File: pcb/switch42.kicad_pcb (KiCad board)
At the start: 2 copper layers, 91 x 55 mm, 27 parts, among them SW1 SW_PUSH, SW10 SW_PUSH, SW2 SW_PUSH, SW3 SW_PUSH, SW4 SW_PUSH, SW5 SW_PUSH, SW6 SW_PUSH, SW8 SW_PUSH, SW9 SW_PUSH, U1 ProMicro

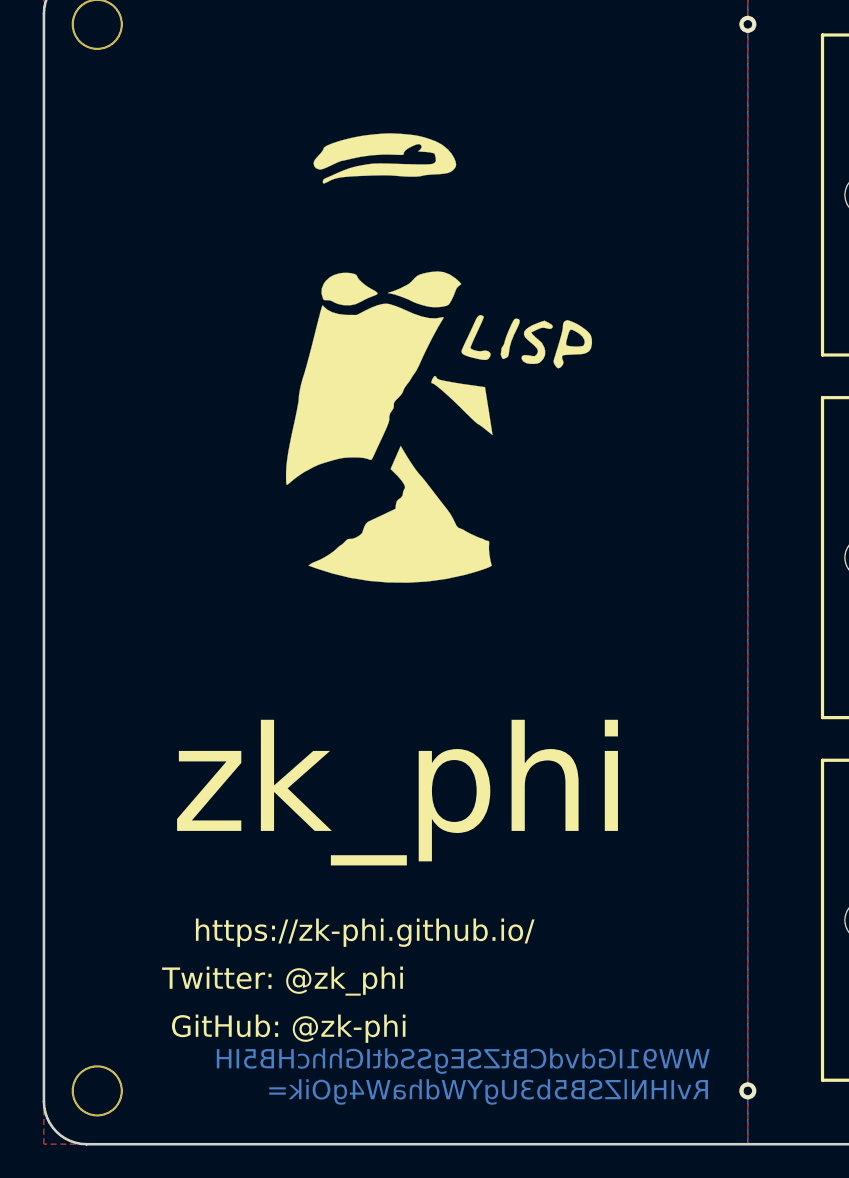
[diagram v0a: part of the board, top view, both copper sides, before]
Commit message: Move meishi contents slightly upward
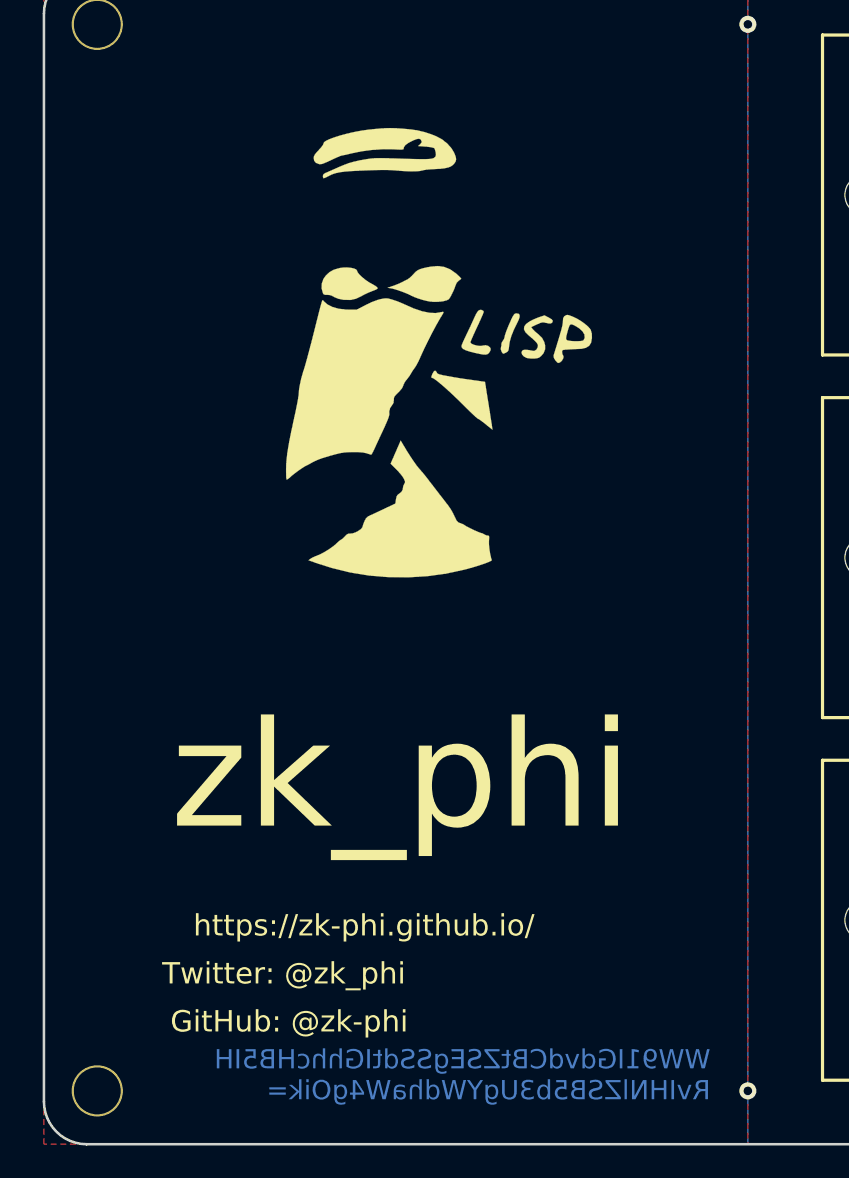
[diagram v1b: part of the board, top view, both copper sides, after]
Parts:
- moved G*** 0.25 mm to (66.8, 66.5) (x2)
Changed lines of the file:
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@@
   )
   (module paripi:Untitled2 (layer F.Cu)
-    (at 66.75 66.75)
+    (at 66.75 66.5)
     (fp_text reference G*** (at 0 0) (layer F.SilkS) hide
       (effects (font (size 1.524 1.524) (thickness 0.3)))
@@
   )
   (module paripi:Untitled (layer F.Cu)
-    (at 66.75 66.75)
+    (at 66.75 66.5)
     (fp_text reference G*** (at 0 0) (layer F.SilkS) hide
       (effects (font (size 1.524 1.524) (thickness 0.3)))
@@
       (xy -0.244517 -0.11784) (xy -0.229978 -0.100089) (xy -0.224367 -0.096087) (xy -0.217842 -0.102074)) (layer B.SilkS) (width 0.01))
   )
-  (gr_text "GitHub: @zk-phi" (at 61.5 99.5) (layer F.SilkS)
+  (gr_text "GitHub: @zk-phi" (at 61.5 99.25) (layer F.SilkS)
     (effects (font (size 1 1) (thickness 0.2)))
   )
-  (gr_text "Twitter: @zk_phi" (at 61.25 97.25) (layer F.SilkS)
+  (gr_text "Twitter: @zk_phi" (at 61.25 97) (layer F.SilkS)
     (effects (font (size 1 1) (thickness 0.2)))
   )
@@
   (gr_line (start 95.75 62.75) (end 95.75 67.25) (layer Edge.Cuts) (width 0.12))
   (gr_line (start 92.25 62.75) (end 95.75 62.75) (layer Edge.Cuts) (width 0.12))
-  (gr_line (start 78.75 100.5) (end 54.75 100.5) (layer Cmts.User) (width 0.6))
-  (gr_line (start 78.75 54.5) (end 78.75 100.5) (layer Cmts.User) (width 0.6))
-  (gr_line (start 54.75 54.5) (end 78.75 54.5) (layer Cmts.User) (width 0.6))
-  (gr_line (start 54.75 100.5) (end 54.75 54.5) (layer Cmts.User) (width 0.6))
-  (gr_text "Software Engineer" (at 66.75 83) (layer F.Mask)
+  (gr_line (start 78.75 100.25) (end 54.75 100.25) (layer Cmts.User) (width 0.6))
+  (gr_line (start 78.75 54.25) (end 78.75 100.25) (layer Cmts.User) (width 0.6))
+  (gr_line (start 54.75 54.25) (end 78.75 54.25) (layer Cmts.User) (width 0.6))
+  (gr_line (start 54.75 100.25) (end 54.75 54.25) (layer Cmts.User) (width 0.6))
+  (gr_text "Software Engineer" (at 66.75 82.75) (layer F.Mask)
     (effects (font (size 1.7 1.7) (thickness 0.3)))
   )
-  (gr_text https://zk-phi.github.io/ (at 65 95) (layer F.SilkS)
+  (gr_text https://zk-phi.github.io/ (at 65 94.75) (layer F.SilkS)
     (effects (font (size 1 1) (thickness 0.2)))
   )
-  (gr_text zk_phi (at 66.75 88) (layer F.SilkS)
+  (gr_text zk_phi (at 66.75 87.75) (layer F.SilkS)
     (effects (font (size 5 5) (thickness 0.7)))
   )

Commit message: Get screw holes plated
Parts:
- Ref** (x4): footprint phi-kbd-library:M2_SCREW_HOLE -> phi-kbd-library:M2_SCREW_HOLE_Plated
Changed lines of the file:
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@@
     (add_net sw9)
+  )
+  (module phi-kbd-library:M2_SCREW_HOLE_Plated (layer F.Cu)
+    (at 138.5 52.5)
+    (descr "Mounting Hole 2.2mm, no annular, M2")
+    (tags "mounting hole 2.2mm no annular m2")
+    (attr virtual)
+    (fp_text reference Ref** (at 0 -3.2) (layer F.Fab)
+      (effects (font (size 1 1) (thickness 0.15)))
+    )
+    (fp_text value Val** (at 0 3.2) (layer F.Fab)
+      (effects (font (size 1 1) (thickness 0.15)))
+    )
+    (fp_circle (center 0 0) (end 0 1.75) (layer F.Fab) (width 0.15))
+    (fp_text user %R (at 0.3 0) (layer F.Fab)
+      (effects (font (size 1 1) (thickness 0.15)))
+    )
+    (pad "" thru_hole circle (at 0 0) (size 2.4 2.4) (drill 2.2) (layers *.Cu *.Mask))
+    (model ${KISYS3DMOD}/phi-kbd.3dshapes/M2_Screw.step
+      (at (xyz 0 0 0))
+      (scale (xyz 1 1 1))
+      (rotate (xyz 0 0 0))
+    )
+  )
+  (module phi-kbd-library:M2_SCREW_HOLE_Plated (layer F.Cu)
+    (at 138.5 102.5)
+    (descr "Mounting Hole 2.2mm, no annular, M2")
+    (tags "mounting hole 2.2mm no annular m2")
+    (attr virtual)
+    (fp_text reference Ref** (at 0 -3.2) (layer F.Fab)
+      (effects (font (size 1 1) (thickness 0.15)))
+    )
+    (fp_text value Val** (at 0 3.2) (layer F.Fab)
+      (effects (font (size 1 1) (thickness 0.15)))
+    )
+    (fp_circle (center 0 0) (end 0 1.75) (layer F.Fab) (width 0.15))
+    (fp_text user %R (at 0.3 0) (layer F.Fab)
+      (effects (font (size 1 1) (thickness 0.15)))
+    )
+    (pad "" thru_hole circle (at 0 0) (size 2.4 2.4) (drill 2.2) (layers *.Cu *.Mask))
+    (model ${KISYS3DMOD}/phi-kbd.3dshapes/M2_Screw.step
+      (at (xyz 0 0 0))
+      (scale (xyz 1 1 1))
+      (rotate (xyz 0 0 0))
+    )
+  )
+  (module phi-kbd-library:M2_SCREW_HOLE_Plated (layer F.Cu)
+    (at 52.5 102.5)
+    (descr "Mounting Hole 2.2mm, no annular, M2")
+    (tags "mounting hole 2.2mm no annular m2")
+    (attr virtual)
+    (fp_text reference Ref** (at 0 -3.2) (layer F.Fab)
+      (effects (font (size 1 1) (thickness 0.15)))
+    )
+    (fp_text value Val** (at 0 3.2) (layer F.Fab)
+      (effects (font (size 1 1) (thickness 0.15)))
+    )
+    (fp_circle (center 0 0) (end 0 1.75) (layer F.Fab) (width 0.15))
+    (fp_text user %R (at 0.3 0) (layer F.Fab)
+      (effects (font (size 1 1) (thickness 0.15)))
+    )
+    (pad "" thru_hole circle (at 0 0) (size 2.4 2.4) (drill 2.2) (layers *.Cu *.Mask))
+    (model ${KISYS3DMOD}/phi-kbd.3dshapes/M2_Screw.step
+      (at (xyz 0 0 0))
+      (scale (xyz 1 1 1))
+      (rotate (xyz 0 0 0))
+    )
+  )
+  (module phi-kbd-library:M2_SCREW_HOLE_Plated (layer F.Cu)
+    (at 52.5 52.5)
+    (descr "Mounting Hole 2.2mm, no annular, M2")
+    (tags "mounting hole 2.2mm no annular m2")
+    (attr virtual)
+    (fp_text reference Ref** (at 0 -3.2) (layer F.Fab)
+      (effects (font (size 1 1) (thickness 0.15)))
+    )
+    (fp_text value Val** (at 0 3.2) (layer F.Fab)
+      (effects (font (size 1 1) (thickness 0.15)))
+    )
+    (fp_circle (center 0 0) (end 0 1.75) (layer F.Fab) (width 0.15))
+    (fp_text user %R (at 0.3 0) (layer F.Fab)
+      (effects (font (size 1 1) (thickness 0.15)))
+    )
+    (pad "" thru_hole circle (at 0 0) (size 2.4 2.4) (drill 2.2) (layers *.Cu *.Mask))
+    (model ${KISYS3DMOD}/phi-kbd.3dshapes/M2_Screw.step
+      (at (xyz 0 0 0))
+      (scale (xyz 1 1 1))
+      (rotate (xyz 0 0 0))
+    )
   )
   (module paripi:Untitled2 (layer F.Cu)
@@
     )
   )
-  (module phi-kbd-library:M2_SCREW_HOLE (layer F.Cu)
-    (at 52.5 52.5)
-    (descr "Mounting Hole 2.2mm, no annular, M2")
-    (tags "mounting hole 2.2mm no annular m2")
-    (attr virtual)
-    (fp_text reference Ref** (at 0 -3.2) (layer F.Fab)
-      (effects (font (size 1 1) (thickness 0.15)))
-    )
-    (fp_text value Val** (at 0 3.2) (layer F.Fab)
-      (effects (font (size 1 1) (thickness 0.15)))
-    )
-    (fp_circle (center 0 0) (end 0 1.75) (layer F.Fab) (width 0.15))
-    (fp_text user %R (at 0.3 0) (layer F.Fab)
-      (effects (font (size 1 1) (thickness 0.15)))
-    )
-    (pad "" np_thru_hole circle (at 0 0) (size 2.4 2.4) (drill 2.2) (layers *.Cu *.Mask))
-    (model ${KISYS3DMOD}/phi-kbd.3dshapes/M2_Screw.step
-      (at (xyz 0 0 0))
-      (scale (xyz 1 1 1))
-      (rotate (xyz 0 0 0))
-    )
-  )
-  (module phi-kbd-library:M2_SCREW_HOLE (layer F.Cu)
-    (at 138.5 52.5)
-    (descr "Mounting Hole 2.2mm, no annular, M2")
-    (tags "mounting hole 2.2mm no annular m2")
-    (attr virtual)
-    (fp_text reference Ref** (at 0 -3.2) (layer F.Fab)
-      (effects (font (size 1 1) (thickness 0.15)))
-    )
-    (fp_text value Val** (at 0 3.2) (layer F.Fab)
-      (effects (font (size 1 1) (thickness 0.15)))
-    )
-    (fp_circle (center 0 0) (end 0 1.75) (layer F.Fab) (width 0.15))
-    (fp_text user %R (at 0.3 0) (layer F.Fab)
-      (effects (font (size 1 1) (thickness 0.15)))
-    )
-    (pad "" np_thru_hole circle (at 0 0) (size 2.4 2.4) (drill 2.2) (layers *.Cu *.Mask))
-    (model ${KISYS3DMOD}/phi-kbd.3dshapes/M2_Screw.step
-      (at (xyz 0 0 0))
-      (scale (xyz 1 1 1))
-      (rotate (xyz 0 0 0))
-    )
-  )
-  (module phi-kbd-library:M2_SCREW_HOLE (layer F.Cu)
-    (at 52.5 102.5)
-    (descr "Mounting Hole 2.2mm, no annular, M2")
-    (tags "mounting hole 2.2mm no annular m2")
-    (attr virtual)
-    (fp_text reference Ref** (at 0 -3.2) (layer F.Fab)
-      (effects (font (size 1 1) (thickness 0.15)))
-    )
-    (fp_text value Val** (at 0 3.2) (layer F.Fab)
-      (effects (font (size 1 1) (thickness 0.15)))
-    )
-    (fp_circle (center 0 0) (end 0 1.75) (layer F.Fab) (width 0.15))
-    (fp_text user %R (at 0.3 0) (layer F.Fab)
-      (effects (font (size 1 1) (thickness 0.15)))
-    )
-    (pad "" np_thru_hole circle (at 0 0) (size 2.4 2.4) (drill 2.2) (layers *.Cu *.Mask))
-    (model ${KISYS3DMOD}/phi-kbd.3dshapes/M2_Screw.step
-      (at (xyz 0 0 0))
-      (scale (xyz 1 1 1))
-      (rotate (xyz 0 0 0))
-    )
-  )
-  (module phi-kbd-library:M2_SCREW_HOLE (layer F.Cu)
-    (at 138.5 102.5)
-    (descr "Mounting Hole 2.2mm, no annular, M2")
-    (tags "mounting hole 2.2mm no annular m2")
-    (attr virtual)
-    (fp_text reference Ref** (at 0 -3.2) (layer F.Fab)
-      (effects (font (size 1 1) (thickness 0.15)))
-    )
-    (fp_text value Val** (at 0 3.2) (layer F.Fab)
-      (effects (font (size 1 1) (thickness 0.15)))
-    )
-    (fp_circle (center 0 0) (end 0 1.75) (layer F.Fab) (width 0.15))
-    (fp_text user %R (at 0.3 0) (layer F.Fab)
-      (effects (font (size 1 1) (thickness 0.15)))
-    )
-    (pad "" np_thru_hole circle (at 0 0) (size 2.4 2.4) (drill 2.2) (layers *.Cu *.Mask))
-    (model ${KISYS3DMOD}/phi-kbd.3dshapes/M2_Screw.step
-      (at (xyz 0 0 0))
-      (scale (xyz 1 1 1))
-      (rotate (xyz 0 0 0))
-    )
-  )
   (module phi-kbd-library:Icon-Scissors (layer B.Cu)
     (at 109.25 54.5 270)
@@
   (gr_line (start 54.75 54.25) (end 78.75 54.25) (layer Cmts.User) (width 0.6))
   (gr_line (start 54.75 100.25) (end 54.75 54.25) (layer Cmts.User) (width 0.6))
-  (gr_text "Software Engineer" (at 66.75 82.75) (layer F.Mask)
+  (gr_text "Software Engineer" (at 66.75 82.5) (layer F.Mask)
     (effects (font (size 1.7 1.7) (thickness 0.3)))
   )

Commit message: Update challenge
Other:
- board text added: "D1"
- board text added: "D2"
- board text added: "D3"
- board text added: "D4"
- board text added: "D5"
- board text added: "D6"
- board text added: "D7"
- board text added: "D8"
- board text added: "D9"
- board text added: "GRID = .25"
- board text added: "“64” and “13” me ! (I = ai) SFVIIDB6ciBMMXINCmdjbiAwY3 QgVDQ0DQp+RiEgcjJhIFpsMQ=="
- board text removed: "WW91IGdvdCBtZSEgSSdtIGhhcHB5IH RvIHNlZSB5b3UgYWdhaW4gOik="
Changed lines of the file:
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@@
   (general
     (thickness 1.6)
-    (drawings 67)
+    (drawings 77)
     (tracks 112)
     (zones 0)
@@
       (xy -0.244517 -0.11784) (xy -0.229978 -0.100089) (xy -0.224367 -0.096087) (xy -0.217842 -0.102074)) (layer B.SilkS) (width 0.01))
   )
+  (gr_text D9 (at 134.75 99) (layer B.SilkS)
+    (effects (font (size 1 1) (thickness 0.2)) (justify mirror))
+  )
+  (gr_text D8 (at 116.75 99) (layer B.SilkS)
+    (effects (font (size 1 1) (thickness 0.2)) (justify mirror))
+  )
+  (gr_text D7 (at 98.75 99) (layer B.SilkS)
+    (effects (font (size 1 1) (thickness 0.2)) (justify mirror))
+  )
+  (gr_text D6 (at 134.75 82) (layer B.SilkS)
+    (effects (font (size 1 1) (thickness 0.2)) (justify mirror))
+  )
+  (gr_text D5 (at 116.75 82) (layer B.SilkS)
+    (effects (font (size 1 1) (thickness 0.2)) (justify mirror))
+  )
+  (gr_text D4 (at 98.75 82) (layer B.SilkS)
+    (effects (font (size 1 1) (thickness 0.2)) (justify mirror))
+  )
+  (gr_text D3 (at 134.75 65) (layer B.SilkS)
+    (effects (font (size 1 1) (thickness 0.2)) (justify mirror))
+  )
+  (gr_text D2 (at 116.75 65) (layer B.SilkS)
+    (effects (font (size 1 1) (thickness 0.2)) (justify mirror))
+  )
+  (gr_text D1 (at 98.75 65) (layer B.SilkS)
+    (effects (font (size 1 1) (thickness 0.2)) (justify mirror))
+  )
+  (gr_text "GRID = .25" (at 133.75 107.75) (layer Dwgs.User)
+    (effects (font (size 1.5 1.5) (thickness 0.3)))
+  )
   (gr_text "GitHub: @zk-phi" (at 61.5 99.25) (layer F.SilkS)
     (effects (font (size 1 1) (thickness 0.2)))
@@
     (effects (font (size 1 0.9) (thickness 0.2)) (justify mirror))
   )
-  (gr_text "WW91IGdvdCBtZSEgSSdtIGhhcHB5IH\nRvIHNlZSB5b3UgYWdhaW4gOik=" (at 81.25 101.75) (layer B.Cu)
+  (gr_text "“64” and “13” me ! (I = ai)\nSFVIIDB6ciBMMXINCmdjbiAwY3\nQgVDQ0DQp+RiEgcjJhIFpsMQ==" (at 81.25 100.75) (layer B.Cu)
     (effects (font (size 0.9 0.9) (thickness 0.2)) (justify left mirror))
   )
@@
   (gr_line (start 54.75 54.25) (end 78.75 54.25) (layer Cmts.User) (width 0.6))
   (gr_line (start 54.75 100.25) (end 54.75 54.25) (layer Cmts.User) (width 0.6))
-  (gr_text "Software Engineer" (at 66.75 82.5) (layer F.Mask)
+  (gr_text "Software Engineer" (at 66.75 82.25) (layer F.Mask)
     (effects (font (size 1.7 1.7) (thickness 0.3)))
   )
@@
     (effects (font (size 1 1) (thickness 0.2)))
   )
-  (gr_text zk_phi (at 66.75 87.75) (layer F.SilkS)
+  (gr_text zk_phi (at 66.75 88) (layer F.SilkS)
     (effects (font (size 5 5) (thickness 0.7)))
   )

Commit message: Update buildguide
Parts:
- removed the G*** at (109.2, 54.5)
- removed the G*** at (114.2, 56.8)
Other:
- board text added: "1. Flash the firmware on a ProMicro available here: https://github.com/zk-phi/qmk_firmware $ sh util/<your_OS>_install.sh $ make handwired/ddm9:default:avrdude 2. Solder x9 SK6812mini LEDs (Optional) * connected in serial D1 > D2 > … 3. Solder x9 Kailh Choc switches * cut pins marked with “X” 4. Plug ProMicro in with “Conthrough”s"
- board text added: "Build your keypad !"
- board text added: "X"
- board text added: "“64” and “13” me ! (I = “ai”) SFVIIDB6ciBMMXINCmdjbiAwY3 QgVDQ0DQp+RiEgcjJhIFpsMQ=="
- board text removed: "1. Flash the firmware on a ProMicro available here: https://github.com/zk-phi/qmk_firmware $ sh util/<your_OS>_install.sh $ make handwired/ddm9:default:avrdude 2. Solder x9 SK6812mini LEDs (Optional) 3. Solder x9 Kailh Choc switches 4. Plug ProMicro in"
- board text removed: "How to build a keypad"
- board text removed: "“64” and “13” me ! (I = ai) SFVIIDB6ciBMMXINCmdjbiAwY3 QgVDQ0DQp+RiEgcjJhIFpsMQ=="
